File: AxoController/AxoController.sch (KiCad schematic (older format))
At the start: 1 part, among them U1 ESP-12E

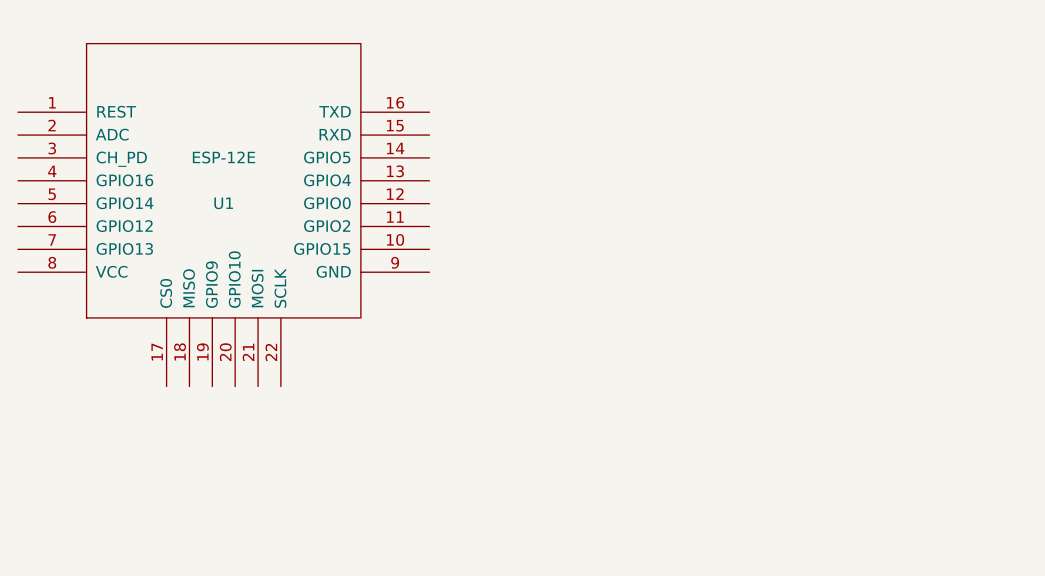
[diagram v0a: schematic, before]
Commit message: Bugfixes
fixed FanRPM
fixed LEDintensity
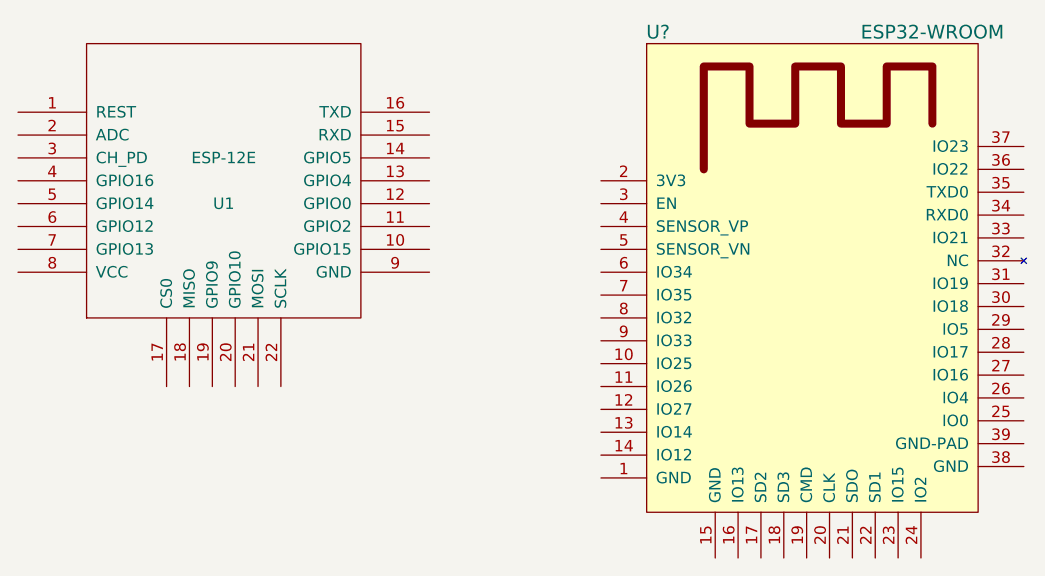
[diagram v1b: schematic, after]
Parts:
- added U?: ESP32-WROOM, ESP32-footprints-Lib:ESP32-WROOM, symbol ESP32-WROOM
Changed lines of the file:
@@
 LIBS:valves
 LIBS:ESP8266
+LIBS:ESP32-footprints-Shem-Lib
 LIBS:AxoController-cache
 EELAYER 25 0
@@
 	1    0    0    -1
 $EndComp
+$Comp
+L ESP32-WROOM U?
+U 1 1 59DA3819
+P 6050 3050
+F 0 "U?" H 5350 4300 60  0000 C CNN
+F 1 "ESP32-WROOM" H 6550 4300 60  0000 C CNN
+F 2 "ESP32-footprints-Lib:ESP32-WROOM" H 6400 4400 60  0001 C CNN
+F 3 "" H 5600 3500 60  0001 C CNN
+	1    6050 3050
+	1    0    0    -1
+$EndComp
